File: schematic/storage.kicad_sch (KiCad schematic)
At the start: 7 parts, among them U2 27C256, U3 SCM2114AL, U4 SCM2114AL

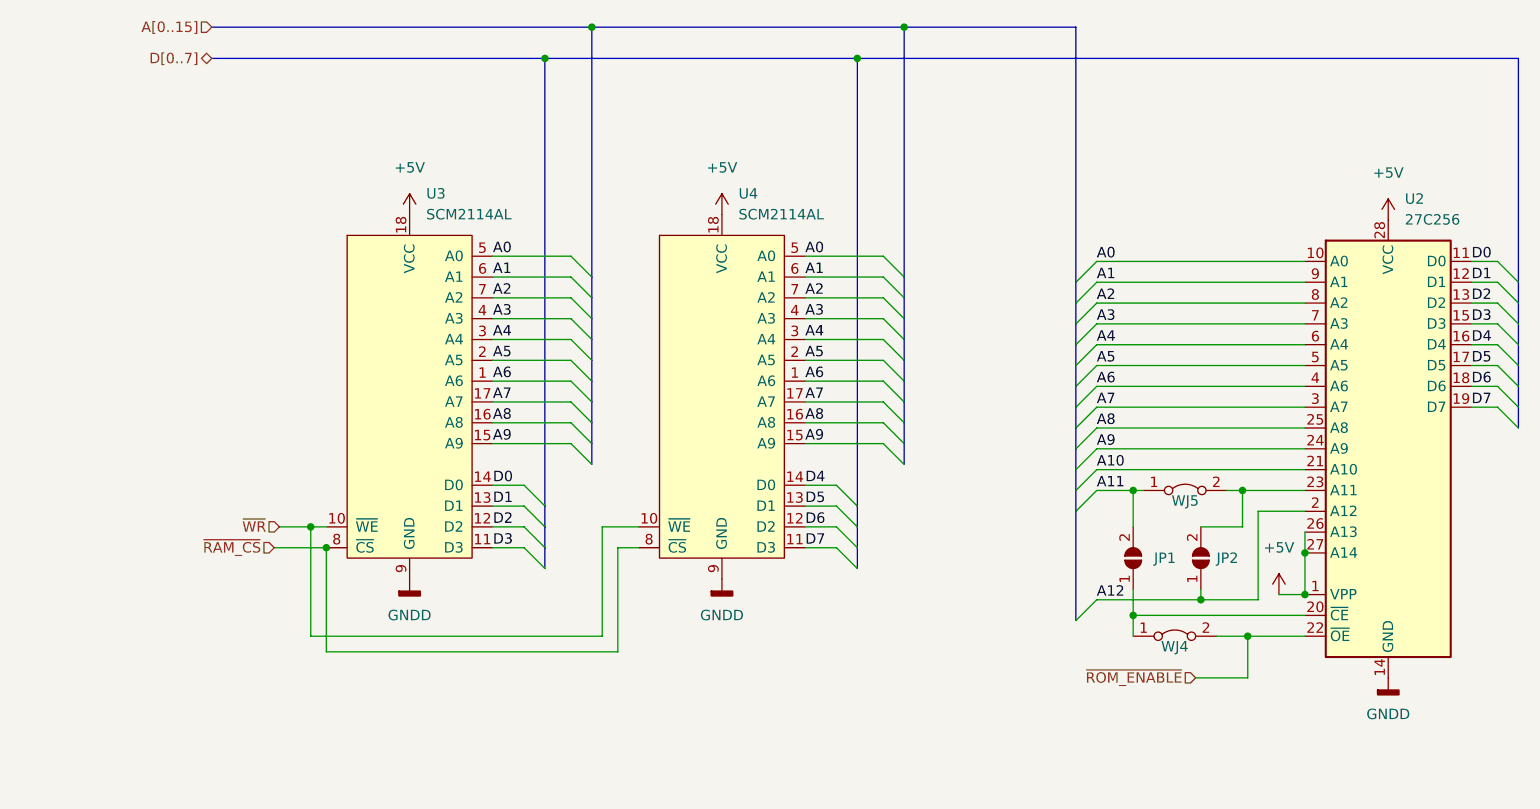
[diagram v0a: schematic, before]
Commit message: altered and did some cleanup of the way the wires were run. Finished expansion port routes to rf modulator. Added ext_psu for future external power supply design (will be an off the shelf psu block).
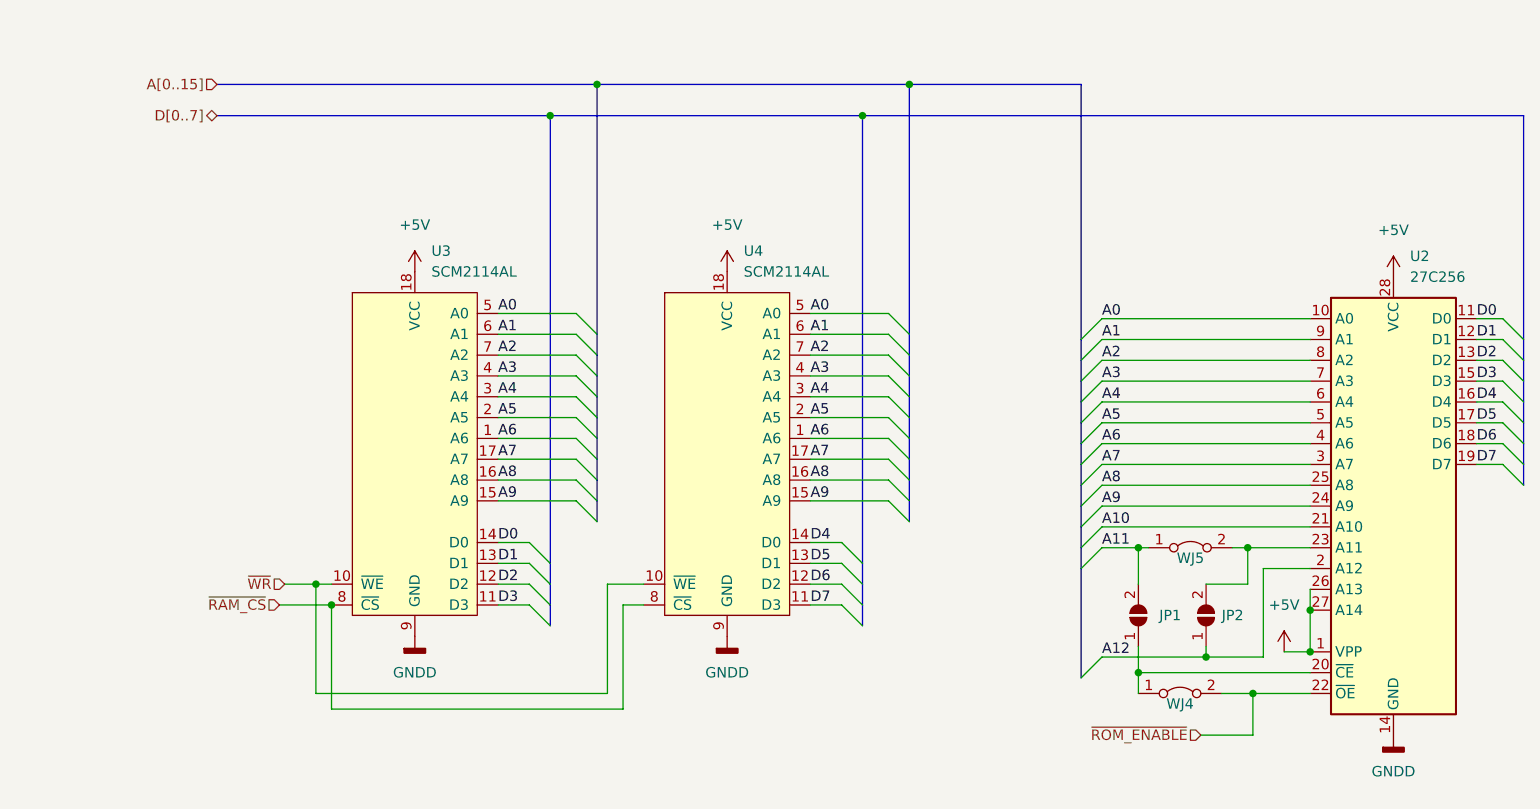
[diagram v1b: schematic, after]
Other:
- moved on the sheet: JP1, JP2, U2, U3, U4, WJ4, WJ5

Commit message: adjusted size of the sheets. added pcb version to the rev field. F.0... the 0 is for future fixes on my end. RF PCB is E.0.
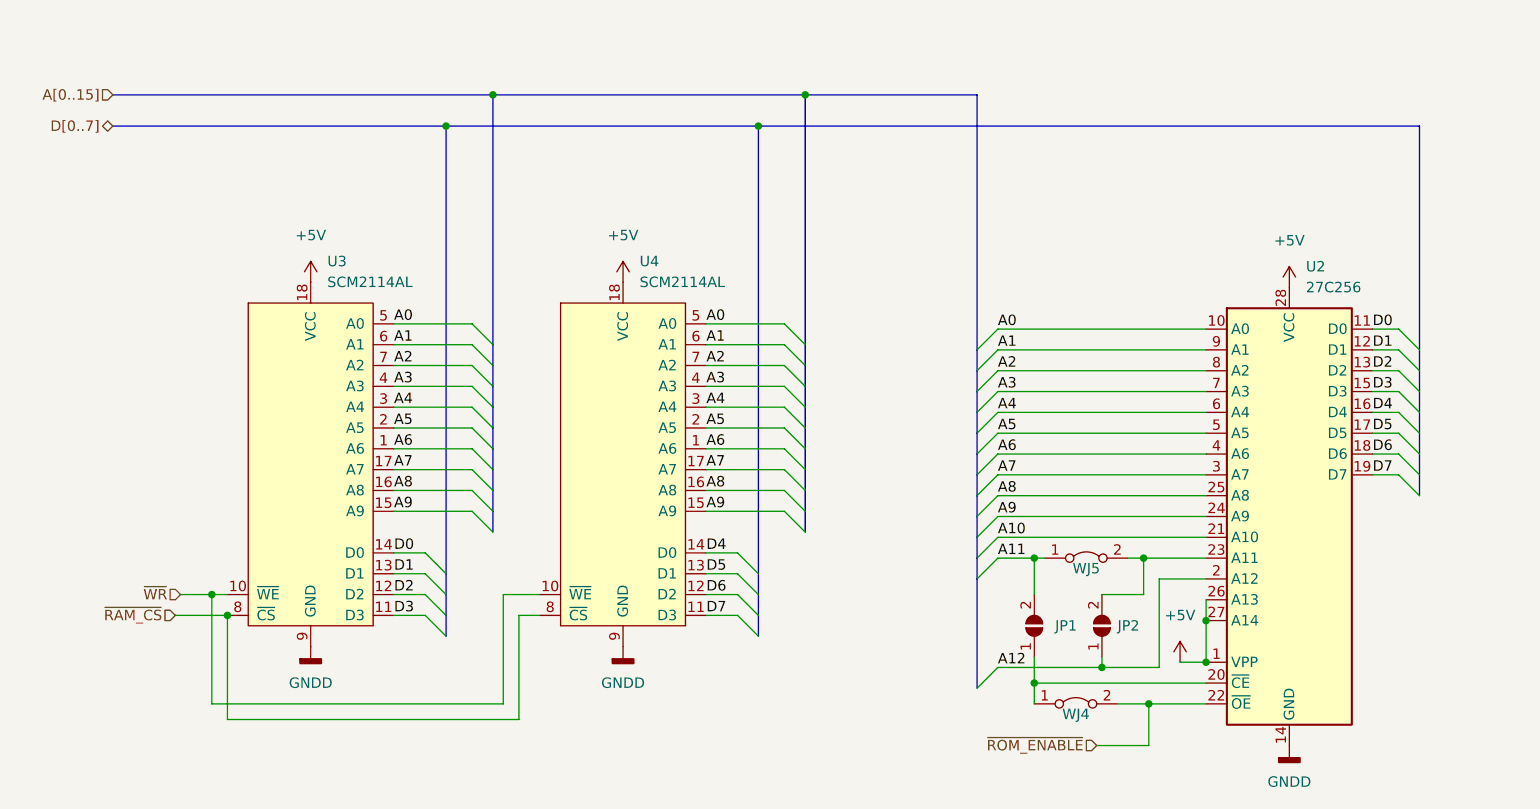
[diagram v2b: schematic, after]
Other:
- title: (none) -> Colecovision Schematic
- moved on the sheet: JP1, JP2, U2, U3, U4, WJ4, WJ5

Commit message: cleanup, and started associating components
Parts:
- JP1, JP2: footprint (none) -> Jumper:SolderJumper-2_P1.3mm_Open_Pad1.0x1.5mm
- U3, U4: footprint (none) -> Package_DIP:DIP-18_W7.62mm_LongPads
- WJ4, WJ5: footprint (none) -> Resistor_THT:R_Bare_Metal_Element_L16.3mm_W4.8mm_P15.30mm
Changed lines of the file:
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@@
       (effects (font (size 1.27 1.27)) (justify left))
     )
-    (property "Footprint" "" (id 2) (at 85.09 84.455 0)
+    (property "Footprint" "Package_DIP:DIP-18_W7.62mm_LongPads" (id 2) (at 85.09 84.455 0)
       (effects (font (size 1.27 1.27)) hide)
     )
@@
   (symbol (lib_id "power:GNDD") (at 204.47 134.62 0) (unit 1)
     (in_bom yes) (on_board yes) (fields_autoplaced)
-    (property "Reference" "#PWR?" (id 0) (at 204.47 140.97 0)
+    (property "Reference" "#PWR0131" (id 0) (at 204.47 140.97 0)
       (effects (font (size 1.27 1.27)) hide)
     )
@@
       (effects (font (size 1.27 1.27)) (justify right) hide)
     )
-    (property "Footprint" "" (id 2) (at 181.61 120.015 0)
+    (property "Footprint" "Jumper:SolderJumper-2_P1.3mm_Open_Pad1.0x1.5mm" (id 2) (at 181.61 120.015 0)
       (effects (font (size 1.27 1.27)) hide)
     )
@@
   (symbol (lib_id "power:+5V") (at 191.135 124.46 0) (unit 1)
     (in_bom yes) (on_board yes) (fields_autoplaced)
-    (property "Reference" "#PWR?" (id 0) (at 191.135 128.27 0)
+    (property "Reference" "#PWR0132" (id 0) (at 191.135 128.27 0)
       (effects (font (size 1.27 1.27)) hide)
     )
@@
   (symbol (lib_id "power:+5V") (at 123.19 78.105 0) (unit 1)
     (in_bom yes) (on_board yes) (fields_autoplaced)
-    (property "Reference" "#PWR?" (id 0) (at 123.19 81.915 0)
+    (property "Reference" "#PWR0130" (id 0) (at 123.19 81.915 0)
       (effects (font (size 1.27 1.27)) hide)
     )
@@
       (effects (font (size 1.27 1.27)) (justify left))
     )
-    (property "Footprint" "" (id 2) (at 123.19 84.455 0)
+    (property "Footprint" "Package_DIP:DIP-18_W7.62mm_LongPads" (id 2) (at 123.19 84.455 0)
       (effects (font (size 1.27 1.27)) hide)
     )
@@
   (symbol (lib_id "power:+5V") (at 85.09 78.105 0) (unit 1)
     (in_bom yes) (on_board yes) (fields_autoplaced)
-    (property "Reference" "#PWR?" (id 0) (at 85.09 81.915 0)
+    (property "Reference" "#PWR0136" (id 0) (at 85.09 81.915 0)
       (effects (font (size 1.27 1.27)) hide)
     )
@@
       (effects (font (size 1.27 1.27)) (justify right) hide)
     )
-    (property "Footprint" "" (id 2) (at 173.355 120.015 0)
+    (property "Footprint" "Jumper:SolderJumper-2_P1.3mm_Open_Pad1.0x1.5mm" (id 2) (at 173.355 120.015 0)
       (effects (font (size 1.27 1.27)) hide)
     )
@@
       (effects (font (size 1.27 1.27)) hide)
     )
-    (property "Footprint" "" (id 2) (at 179.705 111.76 0)
+    (property "Footprint" "Resistor_THT:R_Bare_Metal_Element_L16.3mm_W4.8mm_P15.30mm" (id 2) (at 179.705 111.76 0)
       (effects (font (size 1.27 1.27)) hide)
     )
@@
   (symbol (lib_id "power:+5V") (at 204.47 78.74 0) (unit 1)
     (in_bom yes) (on_board yes) (fields_autoplaced)
-    (property "Reference" "#PWR?" (id 0) (at 204.47 82.55 0)
+    (property "Reference" "#PWR0134" (id 0) (at 204.47 82.55 0)
       (effects (font (size 1.27 1.27)) hide)
     )
@@
   (symbol (lib_id "power:GNDD") (at 85.09 122.555 0) (unit 1)
     (in_bom yes) (on_board yes) (fields_autoplaced)
-    (property "Reference" "#PWR?" (id 0) (at 85.09 128.905 0)
+    (property "Reference" "#PWR0133" (id 0) (at 85.09 128.905 0)
       (effects (font (size 1.27 1.27)) hide)
     )
@@
   (symbol (lib_id "power:GNDD") (at 123.19 122.555 0) (unit 1)
     (in_bom yes) (on_board yes) (fields_autoplaced)
-    (property "Reference" "#PWR?" (id 0) (at 123.19 128.905 0)
+    (property "Reference" "#PWR0135" (id 0) (at 123.19 128.905 0)
       (effects (font (size 1.27 1.27)) hide)
     )
@@
       (effects (font (size 1.27 1.27)) hide)
     )
-    (property "Footprint" "" (id 2) (at 178.435 129.54 0)
-      (effects (font (size 1.27 1.27)) hide)
-    )
+    (property "Footprint" "Resistor_THT:R_Bare_Metal_Element_L16.3mm_W4.8mm_P15.30mm" (id 2) (at 178.435 129.54 0)
+      (effects (font (size 1.27 1.27)) hide)
+    )

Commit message: added new libs for rest of the parts. some still need updating for correct parts, but for now they work. PCB import complete.
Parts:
- WJ4, WJ5: footprint Resistor_THT:R_Bare_Metal_Element_L16.3mm_W4.8mm_P15.30mm -> Resistor_THT:R_Axial_DIN0204_L3.6mm_D1.6mm_P7.62mm_Horizontal
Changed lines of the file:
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@@
       (effects (font (size 1.27 1.27)) hide)
     )
-    (property "Footprint" "Resistor_THT:R_Bare_Metal_Element_L16.3mm_W4.8mm_P15.30mm" (id 2) (at 179.705 111.76 0)
+    (property "Footprint" "Resistor_THT:R_Axial_DIN0204_L3.6mm_D1.6mm_P7.62mm_Horizontal" (id 2) (at 179.705 111.76 0)
       (effects (font (size 1.27 1.27)) hide)
     )
@@
       (effects (font (size 1.27 1.27)) hide)
     )
-    (property "Footprint" "Resistor_THT:R_Bare_Metal_Element_L16.3mm_W4.8mm_P15.30mm" (id 2) (at 178.435 129.54 0)
+    (property "Footprint" "Resistor_THT:R_Axial_DIN0204_L3.6mm_D1.6mm_P7.62mm_Horizontal" (id 2) (at 178.435 129.54 0)
       (effects (font (size 1.27 1.27)) hide)
     )

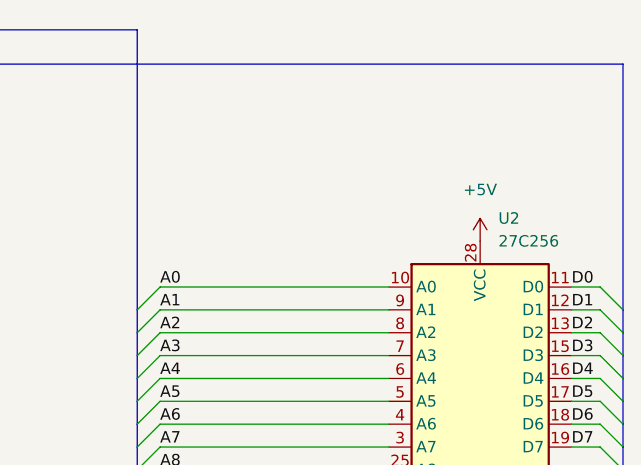
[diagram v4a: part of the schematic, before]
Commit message: first draft of board with components added, no traces
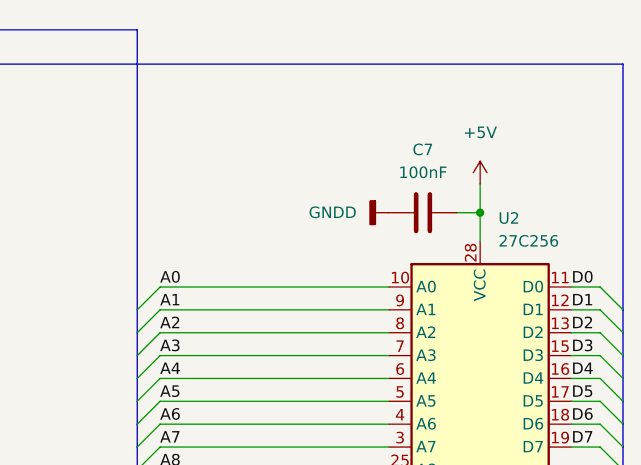
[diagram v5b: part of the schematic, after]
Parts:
- added C7: 100nF, Capacitor_THT:C_Disc_D7.0mm_W2.5mm_P5.00mm, symbol Device:C
- WJ4, WJ5: footprint Resistor_THT:R_Axial_DIN0204_L3.6mm_D1.6mm_P7.62mm_Horizontal -> Resistor_THT:R_Axial_DIN0207_L6.3mm_D2.5mm_P15.24mm_Horizontal
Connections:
- net +5V: now also C7.1
- net GNDD: now also C7.2
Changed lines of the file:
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@@
   (junction (at 107.315 55.245) (diameter 0) (color 0 0 0 0)
   )
+  (junction (at 204.47 75.565) (diameter 0) (color 0 0 0 0)
+  )
   (junction (at 187.325 129.54) (diameter 0) (color 0 0 0 0)
   )
@@
     (stroke (width 0) (type default) (color 0 0 0 0))
   )
+  (wire (pts (xy 201.93 75.565) (xy 204.47 75.565))
+    (stroke (width 0) (type default) (color 0 0 0 0))
+  )
   (wire (pts (xy 173.355 123.825) (xy 173.355 127))
     (stroke (width 0) (type default) (color 0 0 0 0))
@@
     (stroke (width 0) (type default) (color 0 0 0 0))
   )
+  (wire (pts (xy 204.47 72.39) (xy 204.47 75.565))
+    (stroke (width 0) (type default) (color 0 0 0 0))
+  )
   (wire (pts (xy 186.69 111.76) (xy 186.69 116.205))
     (stroke (width 0) (type default) (color 0 0 0 0))
@@
   )
   (wire (pts (xy 168.91 91.44) (xy 194.31 91.44))
+    (stroke (width 0) (type default) (color 0 0 0 0))
+  )
+  (wire (pts (xy 204.47 75.565) (xy 204.47 78.74))
     (stroke (width 0) (type default) (color 0 0 0 0))
   )
@@
     (pin "1")
   )
+  (symbol (lib_id "power:GNDD") (at 194.31 75.565 270) (unit 1)
+    (in_bom yes) (on_board yes)
+    (property "Reference" "#PWR0264" (id 0) (at 187.96 75.565 0)
+      (effects (font (size 1.27 1.27)) hide)
+    )
+    (property "Value" "GNDD" (id 1) (at 185.42 75.565 90)
+      (effects (font (size 1.27 1.27)) (justify left))
+    )
+    (property "Footprint" "" (id 2) (at 194.31 75.565 0)
+      (effects (font (size 1.27 1.27)) hide)
+    )
+    (property "Datasheet" "" (id 3) (at 194.31 75.565 0)
+      (effects (font (size 1.27 1.27)) hide)
+    )
+    (pin "1")
+  )
   (symbol (lib_id "power:+5V") (at 123.19 78.105 0) (unit 1)
     (in_bom yes) (on_board yes) (fields_autoplaced)
@@
     (pin "9")
   )
+  (symbol (lib_id "Device:C") (at 198.12 75.565 270) (unit 1)
+    (in_bom yes) (on_board yes) (fields_autoplaced)
+    (property "Reference" "C7" (id 0) (at 198.12 68.58 90))
+    (property "Value" "100nF" (id 1) (at 198.12 71.12 90))
+    (property "Footprint" "Capacitor_THT:C_Disc_D7.0mm_W2.5mm_P5.00mm" (id 2) (at 194.31 76.5302 0)
+      (effects (font (size 1.27 1.27)) hide)
+    )
+    (property "Datasheet" "~" (id 3) (at 198.12 75.565 0)
+      (effects (font (size 1.27 1.27)) hide)
+    )
+    (pin "1")
+    (pin "2")
+  )
   (symbol (lib_id "power:+5V") (at 85.09 78.105 0) (unit 1)
     (in_bom yes) (on_board yes) (fields_autoplaced)
@@
       (effects (font (size 1.27 1.27)) hide)
     )
-    (property "Footprint" "Resistor_THT:R_Axial_DIN0204_L3.6mm_D1.6mm_P7.62mm_Horizontal" (id 2) (at 179.705 111.76 0)
+    (property "Footprint" "Resistor_THT:R_Axial_DIN0207_L6.3mm_D2.5mm_P15.24mm_Horizontal" (id 2) (at 179.705 111.76 0)
       (effects (font (size 1.27 1.27)) hide)
     )
@@
     (pin "2")
   )
-  (symbol (lib_id "power:+5V") (at 204.47 78.74 0) (unit 1)
-    (in_bom yes) (on_board yes) (fields_autoplaced)
-    (property "Reference" "#PWR0134" (id 0) (at 204.47 82.55 0)
-      (effects (font (size 1.27 1.27)) hide)
-    )
-    (property "Value" "+5V" (id 1) (at 204.47 73.025 0))
-    (property "Footprint" "" (id 2) (at 204.47 78.74 0)
-      (effects (font (size 1.27 1.27)) hide)
-    )
-    (property "Datasheet" "" (id 3) (at 204.47 78.74 0)
+  (symbol (lib_id "power:+5V") (at 204.47 72.39 0) (unit 1)
+    (in_bom yes) (on_board yes) (fields_autoplaced)
+    (property "Reference" "#PWR0134" (id 0) (at 204.47 76.2 0)
+      (effects (font (size 1.27 1.27)) hide)
+    )
+    (property "Value" "+5V" (id 1) (at 204.47 66.675 0))
+    (property "Footprint" "" (id 2) (at 204.47 72.39 0)
+      (effects (font (size 1.27 1.27)) hide)
+    )
+    (property "Datasheet" "" (id 3) (at 204.47 72.39 0)
       (effects (font (size 1.27 1.27)) hide)
     )
@@
       (effects (font (size 1.27 1.27)) hide)
     )
-    (property "Footprint" "Resistor_THT:R_Axial_DIN0204_L3.6mm_D1.6mm_P7.62mm_Horizontal" (id 2) (at 178.435 129.54 0)
-      (effects (font (size 1.27 1.27)) hide)
-    )
+    (property "Footprint" "Resistor_THT:R_Axial_DIN0207_L6.3mm_D2.5mm_P15.24mm_Horizontal" (id 2) (at 178.435 129.54 0)
+      (effects (font (size 1.27 1.27)) hide)
+    )

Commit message: updated schematic with new layout
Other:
- company: (none) -> sparkletron
- title: Colecovision Schematic -> Reverse Engineer Colecovision
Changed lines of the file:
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@@
   (paper "USLetter")
   (title_block
-    (title "Colecovision Schematic")
-    (date "2023-01-09")
-    (rev "F.0")
+    (title "Reverse Engineer Colecovision")
+    (date "2023-03-14")
+    (rev "DEV")
+    (company "sparkletron")
     (comment 1 "Jay Convertino")
+    (comment 2 "MIT LICENSE")
   )
   (junction (at 181.61 125.095) (diameter 0) (color 0 0 0 0)
